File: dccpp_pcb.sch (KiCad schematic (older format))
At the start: 53 parts, among them J1 USB_B_Micro, J10 OSTTC022162, J11 OSTTC022162, J12 OSTTC022162, J2 AVR-ISP-6, J3 OSTTC022162, J4 OSTTC022162, J5 OSTTC022162, J6 OSTTC022162, J7 OSTTC022162, J8 OSTTC022162, J9 OSTTC022162, U1 ATmega32U4-AU, U2 74HC04, U3 IFX007T, U4 IFX007T, U5 IFX007T, U6 IFX007T, Y1 Crystal_Small

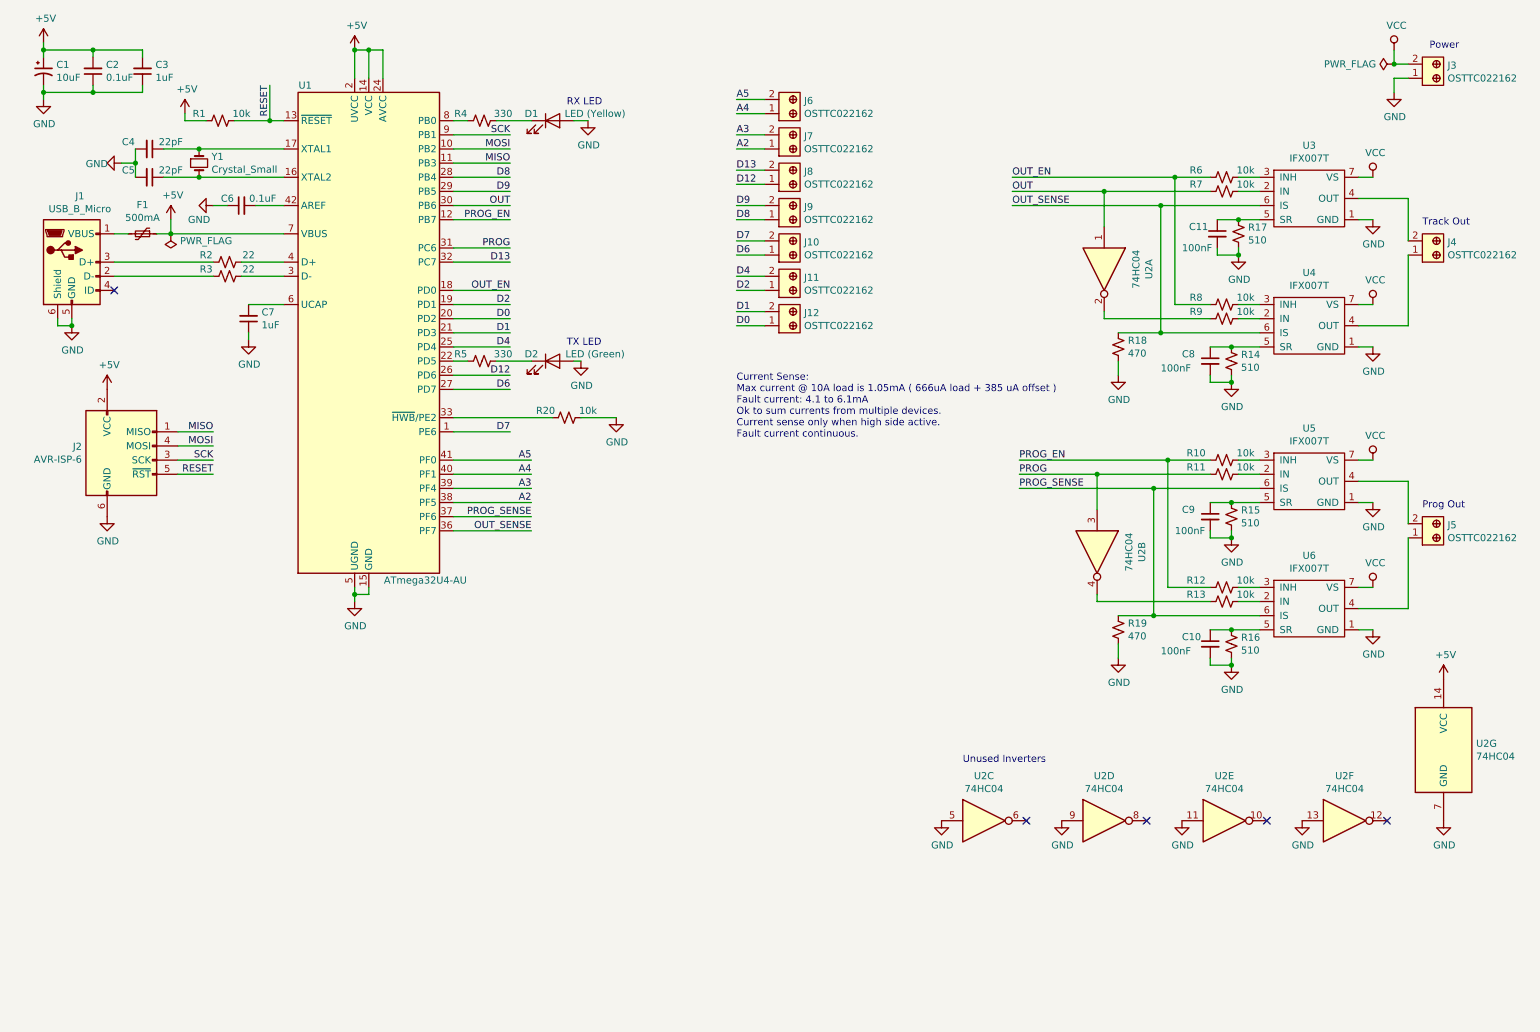
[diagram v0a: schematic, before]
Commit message: Start assigning footprints and part numbers
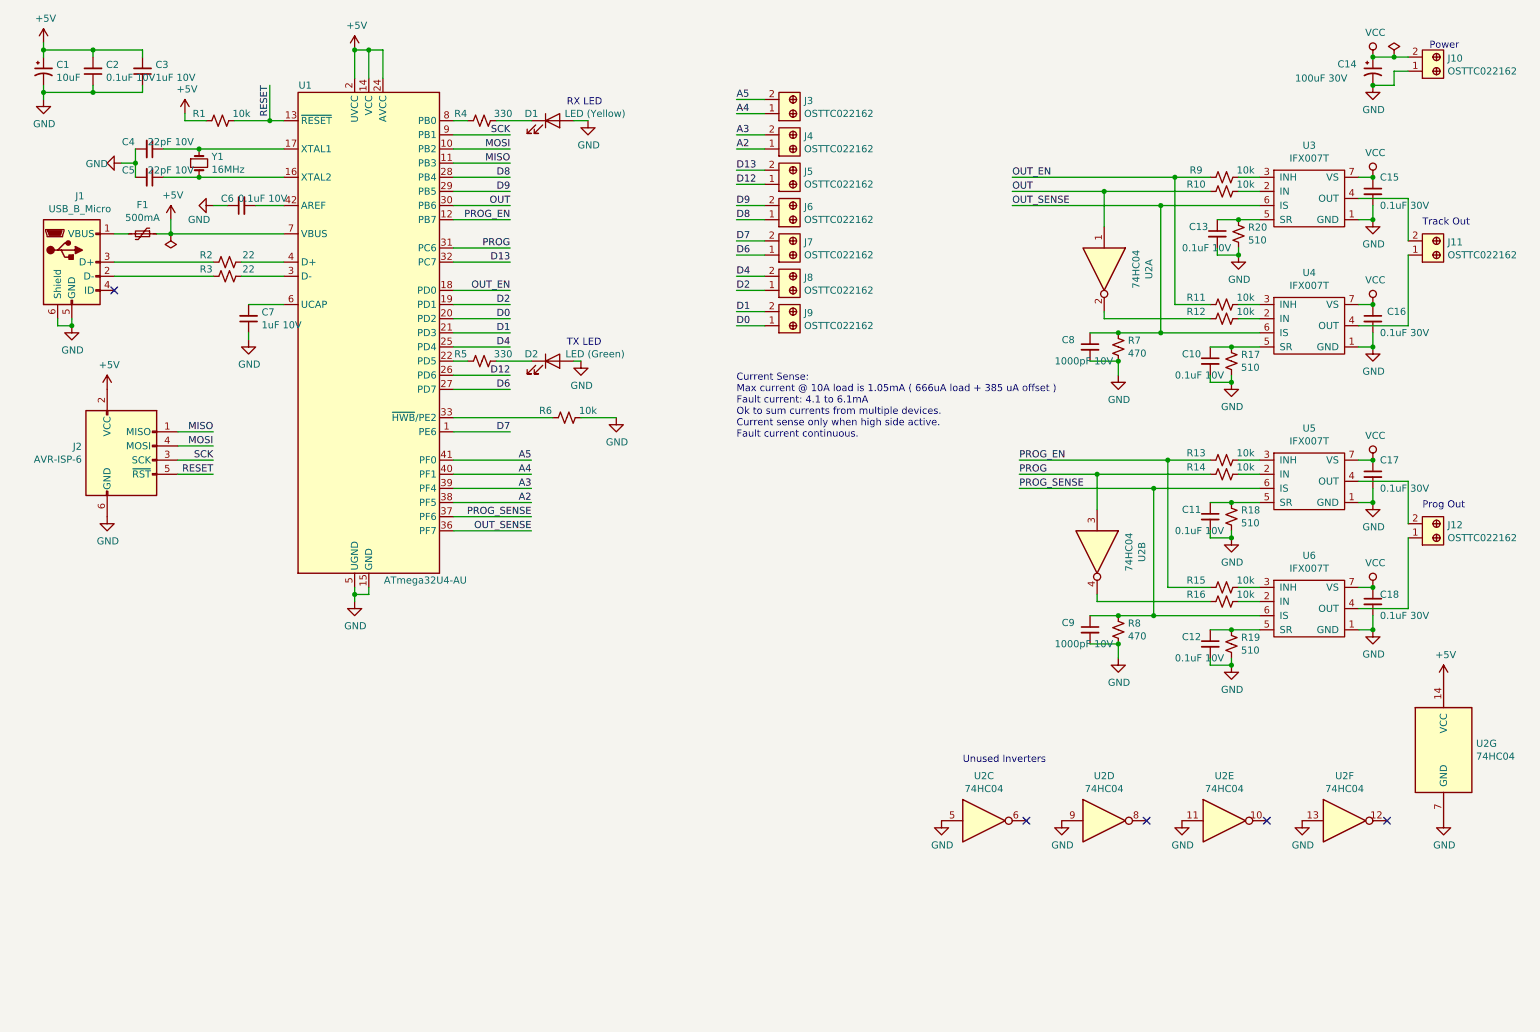
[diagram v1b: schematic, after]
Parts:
- added C14: 100uF 30V, symbol Device:CP1_Small
- added C15, C16, C17, C18: 0.1uF 30V, Capacitor_SMD:C_0603_1608Metric_Pad1.05x0.95mm_HandSolder, symbol Device:C_Small
- added C8, C9: 1000pF 10V, Capacitor_SMD:C_0603_1608Metric_Pad1.05x0.95mm_HandSolder, symbol Device:C_Small
- C1: footprint (none) -> Capacitor_SMD:CP_Elec_4x5.4; Digi-Key_PN (none) -> 732-6401-1-ND; MPN (none) -> 875105240001
- C10: renamed from C8; value 100nF -> 0.1uF 10V; Digi-Key_PN (none) -> 1276-1000-1-ND; MPN (none) -> CL10B104KB8NNNC
- C11: renamed from C9; value 100nF -> 0.1uF 10V; Digi-Key_PN (none) -> 1276-1000-1-ND; MPN (none) -> CL10B104KB8NNNC
- C12: renamed from C10; value 100nF -> 0.1uF 10V; Digi-Key_PN (none) -> 1276-1000-1-ND; MPN (none) -> CL10B104KB8NNNC
- C13: renamed from C11; value 100nF -> 0.1uF 10V; Digi-Key_PN (none) -> 1276-1000-1-ND; MPN (none) -> CL10B104KB8NNNC
- C2, C6: value 0.1uF -> 0.1uF 10V; Digi-Key_PN (none) -> 1276-1000-1-ND; MPN (none) -> CL10B104KB8NNNC
- C3, C7: value 1uF -> 1uF 10V
- C4, C5: value 22pF -> 22pF 10V
- J1: footprint (none) -> Connector_USB:USB_Micro-B_Molex-105017-0001; Digi-Key_PN (none) -> WM1399CT-ND; MPN (none) -> 1050170001
- U1: Digi-Key_PN (none) -> ATMEGA32U4-AU-ND; MPN (none) -> ATMEGA32U4-AU
- U2: footprint (none) -> Package_SO:SOIC-14_3.9x8.7mm_P1.27mm; Digi-Key_PN (none) -> MC74HC04ADGOS-ND; MPN (none) -> MC74HC04ADG
- U3, U4, U5, U6: Digi-Key_PN (none) -> IFX007TAUMA1CT-ND; MPN (none) -> IFX007TAUMA1
- Y1: value Crystal_Small -> 16MHz; footprint (none) -> Crystal:Crystal_SMD_SeikoEpson_TSX3225-4Pin_3.2x2.5mm_HandSoldering; Digi-Key_PN (none) -> SER4069CT-ND; MPN (none) -> TSX-3225 16.0000MF09Z-AC0
- renumbered J3 to J10, J4 to J11, J5 to J12, J6 to J3, J7 to J4, J8 to J5, J9 to J6, J10 to J7, J11 to J8, J12 to J9, R7 to R10, R8 to R11, R9 to R12, R10 to R13, R11 to R14, R12 to R15, R13 to R16, R14 to R17, R15 to R18, R16 to R19, R17 to R20, R20 to R6, R18 to R7, R19 to R8, R6 to R9
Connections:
- net GND: now also C14.2, C15.2, C16.2, C17.2, C18.2, C8.2, C9.2
- net OUT_SENSE: now also C8.1
- net PROG_SENSE: now also C9.1
- net VCC: now also C14.1, C15.1, C16.1, C17.1, C18.1
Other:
- moved on the sheet: J10

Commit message: More part numbers and footprints
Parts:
- C14: footprint (none) -> Capacitor_SMD:CP_Elec_10x10.5; Digi-Key_PN (none) -> 565-4786-1-ND; MPN (none) -> HHXC500ARA101MJA0G
- C3, C7: Digi-Key_PN (none) -> 1276-1182-1-ND; MPN (none) -> CL10A105KP8NNNC
- C4, C5: Digi-Key_PN (none) -> 478-1167-1-ND; MPN (none) -> 06035A220JAT2A
- C8, C9: Digi-Key_PN (none) -> 1276-1018-1-ND; MPN (none) -> CL10B102KB8NNNC
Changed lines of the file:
@@
 F 2 "Capacitor_SMD:C_0603_1608Metric_Pad1.05x0.95mm_HandSolder" H 1450 1700 50  0001 C CNN
 F 3 "~" H 1450 1700 50  0001 C CNN
+F 4 "478-1167-1-ND" H 1450 1700 50  0001 C CNN "Digi-Key_PN"
+F 5 "06035A220JAT2A" H 1450 1700 50  0001 C CNN "MPN"
 	1    1450 1700
 	0    1    1    0
@@
 F 2 "Capacitor_SMD:C_0603_1608Metric_Pad1.05x0.95mm_HandSolder" H 1450 1500 50  0001 C CNN
 F 3 "~" H 1450 1500 50  0001 C CNN
+F 4 "478-1167-1-ND" H 1450 1500 50  0001 C CNN "Digi-Key_PN"
+F 5 "06035A220JAT2A" H 1450 1500 50  0001 C CNN "MPN"
 	1    1450 1500
 	0    1    1    0
@@
 F 2 "Capacitor_SMD:C_0603_1608Metric_Pad1.05x0.95mm_HandSolder" H 2150 2700 50  0001 C CNN
 F 3 "~" H 2150 2700 50  0001 C CNN
+F 4 "1276-1182-1-ND" H 2150 2700 50  0001 C CNN "Digi-Key_PN"
+F 5 "CL10A105KP8NNNC" H 2150 2700 50  0001 C CNN "MPN"
 	1    2150 2700
 	-1   0    0    1
@@
 F 2 "Capacitor_SMD:C_0603_1608Metric_Pad1.05x0.95mm_HandSolder" H 1400 950 50  0001 C CNN
 F 3 "~" H 1400 950 50  0001 C CNN
+F 4 "1276-1182-1-ND" H 1400 950 50  0001 C CNN "Digi-Key_PN"
+F 5 "CL10A105KP8NNNC" H 1400 950 50  0001 C CNN "MPN"
 	1    1400 950
 	-1   0    0    1
@@
 F 2 "Capacitor_SMD:C_0603_1608Metric_Pad1.05x0.95mm_HandSolder" H 8100 4900 50  0001 C CNN
 F 3 "~" H 8100 4900 50  0001 C CNN
+F 4 "1276-1018-1-ND" H 8100 4900 50  0001 C CNN "Digi-Key_PN"
+F 5 "CL10B102KB8NNNC" H 8100 4900 50  0001 C CNN "MPN"
 	1    8100 4900
 	1    0    0    -1
@@
 F 2 "Capacitor_SMD:C_0603_1608Metric_Pad1.05x0.95mm_HandSolder" H 8100 2900 50  0001 C CNN
 F 3 "~" H 8100 2900 50  0001 C CNN
+F 4 "1276-1018-1-ND" H 8100 2900 50  0001 C CNN "Digi-Key_PN"
+F 5 "CL10B102KB8NNNC" H 8100 2900 50  0001 C CNN "MPN"
 	1    8100 2900
 	1    0    0    -1
@@
 F 0 "C14" H 9850 1000 50  0000 L CNN
 F 1 "100uF 30V" H 9550 900 50  0000 L CNN
-F 2 "" H 10100 950 50  0001 C CNN
+F 2 "Capacitor_SMD:CP_Elec_10x10.5" H 10100 950 50  0001 C CNN
 F 3 "~" H 10100 950 50  0001 C CNN
+F 4 "565-4786-1-ND" H 10100 950 50  0001 C CNN "Digi-Key_PN"
+F 5 "HHXC500ARA101MJA0G" H 10100 950 50  0001 C CNN "MPN"
 	1    10100 950
 	1    0    0    -1

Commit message: Final part numbers
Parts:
- D1: Digi-Key_PN (none) -> 732-12018-1-ND; MPN (none) -> 150060YS55040
- D2: Digi-Key_PN (none) -> 732-12017-1-ND; MPN (none) -> 150060VS55040
- F1: value 500mA -> 500mA cont / 1A trip; footprint (none) -> Fuse:Fuse_1206_3216Metric_Pad1.42x1.75mm_HandSolder; Digi-Key_PN (none) -> 507-1802-1-ND; MPN (none) -> 0ZCJ0050FF2G
- J2: Digi-Key_PN (none) -> 609-5122-ND; MPN (none) -> 75869-331LF
- R1, R10, R11, R12, R13, R14, R15, R16, R6, R9: Digi-Key_PN (none) -> RNCP0603FTD10K0CT-ND; MPN (none) -> RNCP0603FTD10K0
- R17, R18, R19, R20: Digi-Key_PN (none) -> 311-510HRCT-ND; MPN (none) -> RC0603FR-07510RL
- R2, R3: Digi-Key_PN (none) -> 311-22.0HRCT-ND; MPN (none) -> RC0603FR-0722RL
- R4, R5: Digi-Key_PN (none) -> 311-330HRCT-ND; MPN (none) -> RC0603FR-07330RL
- R7, R8: Digi-Key_PN (none) -> 311-470HRCT-ND; MPN (none) -> RC0603FR-07470RL
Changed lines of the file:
@@
 F 2 "Resistor_SMD:R_0603_1608Metric_Pad1.05x0.95mm_HandSolder" H 2000 2400 50  0001 C CNN
 F 3 "~" H 2000 2400 50  0001 C CNN
+F 4 "311-22.0HRCT-ND" H 2000 2400 50  0001 C CNN "Digi-Key_PN"
+F 5 "RC0603FR-0722RL" H 2000 2400 50  0001 C CNN "MPN"
 	1    2000 2400
 	0    1    1    0
@@
 P 1400 2100
 F 0 "F1" V 1195 2100 50  0000 C CNN
-F 1 "500mA" V 1286 2100 50  0000 C CNN
-F 2 "" H 1450 1900 50  0001 L CNN
+F 1 "500mA cont / 1A trip" V 1286 2100 50  0000 C CNN
+F 2 "Fuse:Fuse_1206_3216Metric_Pad1.42x1.75mm_HandSolder" H 1450 1900 50  0001 L CNN
 F 3 "~" H 1400 2100 50  0001 C CNN
+F 4 "507-1802-1-ND" H 1400 2100 50  0001 C CNN "Digi-Key_PN"
+F 5 "0ZCJ0050FF2G" H 1400 2100 50  0001 C CNN "MPN"
 	1    1400 2100
 	0    1    1    0
@@
 F 2 "Resistor_SMD:R_0603_1608Metric_Pad1.05x0.95mm_HandSolder" H 1950 1300 50  0001 C CNN
 F 3 "~" H 1950 1300 50  0001 C CNN
+F 4 "RNCP0603FTD10K0CT-ND" H 1950 1300 50  0001 C CNN "Digi-Key_PN"
+F 5 "RNCP0603FTD10K0" H 1950 1300 50  0001 C CNN "MPN"
 	1    1950 1300
 	0    1    1    0
@@
 F 2 "Resistor_SMD:R_0603_1608Metric_Pad1.05x0.95mm_HandSolder" H 2000 2300 50  0001 C CNN
 F 3 "~" H 2000 2300 50  0001 C CNN
+F 4 "311-22.0HRCT-ND" H 2000 2300 50  0001 C CNN "Digi-Key_PN"
+F 5 "RC0603FR-0722RL" H 2000 2300 50  0001 C CNN "MPN"
 	1    2000 2300
 	0    1    1    0
@@
 F 2 "Connector_IDC:IDC-Header_2x03_P2.54mm_Vertical" V 1000 3750 50  0001 C CNN
 F 3 " ~" H -25 3150 50  0001 C CNN
+F 4 "609-5122-ND" H 1250 3700 50  0001 C CNN "Digi-Key_PN"
+F 5 "75869-331LF" H 1250 3700 50  0001 C CNN "MPN"
 	1    1250 3700
 	1    0    0    -1
@@
 F 2 "Resistor_SMD:R_0603_1608Metric_Pad1.05x0.95mm_HandSolder" H 9150 2100 50  0001 C CNN
 F 3 "~" H 9150 2100 50  0001 C CNN
+F 4 "311-510HRCT-ND" H 9150 2100 50  0001 C CNN "Digi-Key_PN"
+F 5 "RC0603FR-07510RL" H 9150 2100 50  0001 C CNN "MPN"
 	1    9150 2100
 	1    0    0    -1
@@
 F 2 "Resistor_SMD:R_0603_1608Metric_Pad1.05x0.95mm_HandSolder" H 9100 3000 50  0001 C CNN
 F 3 "~" H 9100 3000 50  0001 C CNN
+F 4 "311-510HRCT-ND" H 9100 3000 50  0001 C CNN "Digi-Key_PN"
+F 5 "RC0603FR-07510RL" H 9100 3000 50  0001 C CNN "MPN"
 	1    9100 3000
 	1    0    0    -1
@@
 F 2 "Resistor_SMD:R_0603_1608Metric_Pad1.05x0.95mm_HandSolder" H 9100 4100 50  0001 C CNN
 F 3 "~" H 9100 4100 50  0001 C CNN
+F 4 "311-510HRCT-ND" H 9100 4100 50  0001 C CNN "Digi-Key_PN"
+F 5 "RC0603FR-07510RL" H 9100 4100 50  0001 C CNN "MPN"
 	1    9100 4100
 	1    0    0    -1
@@
 F 2 "Resistor_SMD:R_0603_1608Metric_Pad1.05x0.95mm_HandSolder" H 9100 5000 50  0001 C CNN
 F 3 "~" H 9100 5000 50  0001 C CNN
+F 4 "311-510HRCT-ND" H 9100 5000 50  0001 C CNN "Digi-Key_PN"
+F 5 "RC0603FR-07510RL" H 9100 5000 50  0001 C CNN "MPN"
 	1    9100 5000
 	1    0    0    -1
@@
 F 2 "Resistor_SMD:R_0603_1608Metric_Pad1.05x0.95mm_HandSolder" H 9050 1700 50  0001 C CNN
 F 3 "~" H 9050 1700 50  0001 C CNN
+F 4 "RNCP0603FTD10K0CT-ND" H 9050 1700 50  0001 C CNN "Digi-Key_PN"
+F 5 "RNCP0603FTD10K0" H 9050 1700 50  0001 C CNN "MPN"
 	1    9050 1700
 	0    1    1    0
@@
 F 2 "Resistor_SMD:R_0603_1608Metric_Pad1.05x0.95mm_HandSolder" H 9050 1800 50  0001 C CNN
 F 3 "~" H 9050 1800 50  0001 C CNN
+F 4 "RNCP0603FTD10K0CT-ND" H 9050 1800 50  0001 C CNN "Digi-Key_PN"
+F 5 "RNCP0603FTD10K0" H 9050 1800 50  0001 C CNN "MPN"
 	1    9050 1800
 	0    1    1    0
@@
 F 2 "Resistor_SMD:R_0603_1608Metric_Pad1.05x0.95mm_HandSolder" H 9050 2600 50  0001 C CNN
 F 3 "~" H 9050 2600 50  0001 C CNN
+F 4 "RNCP0603FTD10K0CT-ND" H 9050 2600 50  0001 C CNN "Digi-Key_PN"
+F 5 "RNCP0603FTD10K0" H 9050 2600 50  0001 C CNN "MPN"
 	1    9050 2600
 	0    1    1    0
@@
 F 2 "Resistor_SMD:R_0603_1608Metric_Pad1.05x0.95mm_HandSolder" H 9050 2700 50  0001 C CNN
 F 3 "~" H 9050 2700 50  0001 C CNN
+F 4 "RNCP0603FTD10K0CT-ND" H 9050 2700 50  0001 C CNN "Digi-Key_PN"
+F 5 "RNCP0603FTD10K0" H 9050 2700 50  0001 C CNN "MPN"
 	1    9050 2700
 	0    1    1    0
@@
 F 2 "Resistor_SMD:R_0603_1608Metric_Pad1.05x0.95mm_HandSolder" H 9050 3700 50  0001 C CNN
 F 3 "~" H 9050 3700 50  0001 C CNN
+F 4 "RNCP0603FTD10K0CT-ND" H 9050 3700 50  0001 C CNN "Digi-Key_PN"
+F 5 "RNCP0603FTD10K0" H 9050 3700 50  0001 C CNN "MPN"
 	1    9050 3700
 	0    1    1    0
@@
 F 2 "Resistor_SMD:R_0603_1608Metric_Pad1.05x0.95mm_HandSolder" H 9050 3800 50  0001 C CNN
 F 3 "~" H 9050 3800 50  0001 C CNN
+F 4 "RNCP0603FTD10K0CT-ND" H 9050 3800 50  0001 C CNN "Digi-Key_PN"
+F 5 "RNCP0603FTD10K0" H 9050 3800 50  0001 C CNN "MPN"
 	1    9050 3800
 	0    1    1    0
@@
 F 2 "Resistor_SMD:R_0603_1608Metric_Pad1.05x0.95mm_HandSolder" H 9050 4600 50  0001 C CNN
 F 3 "~" H 9050 4600 50  0001 C CNN
+F 4 "RNCP0603FTD10K0CT-ND" H 9050 4600 50  0001 C CNN "Digi-Key_PN"
+F 5 "RNCP0603FTD10K0" H 9050 4600 50  0001 C CNN "MPN"
 	1    9050 4600
 	0    1    1    0
@@
 F 2 "Resistor_SMD:R_0603_1608Metric_Pad1.05x0.95mm_HandSolder" H 9050 4700 50  0001 C CNN
 F 3 "~" H 9050 4700 50  0001 C CNN
+F 4 "RNCP0603FTD10K0CT-ND" H 9050 4700 50  0001 C CNN "Digi-Key_PN"
+F 5 "RNCP0603FTD10K0" H 9050 4700 50  0001 C CNN "MPN"
 	1    9050 4700
 	0    1    1    0
@@
 F 2 "LED_SMD:LED_0603_1608Metric_Pad1.05x0.95mm_HandSolder" H 4300 3000 50  0001 C CNN
 F 3 "~" H 4300 3000 50  0001 C CNN
+F 4 "732-12017-1-ND" H 4300 3000 50  0001 C CNN "Digi-Key_PN"
+F 5 "150060VS55040" H 4300 3000 50  0001 C CNN "MPN"
 	1    4300 3000
 	1    0    0    -1
@@
 F 2 "Resistor_SMD:R_0603_1608Metric_Pad1.05x0.95mm_HandSolder" H 3800 3000 50  0001 C CNN
 F 3 "~" H 3800 3000 50  0001 C CNN
+F 4 "311-330HRCT-ND" H 3800 3000 50  0001 C CNN "Digi-Key_PN"
+F 5 "RC0603FR-07330RL" H 3800 3000 50  0001 C CNN "MPN"
 	1    3800 3000
 	0    1    1    0
@@
 F 2 "Resistor_SMD:R_0603_1608Metric_Pad1.05x0.95mm_HandSolder" H 3800 1300 50  0001 C CNN
 F 3 "~" H 3800 1300 50  0001 C CNN
+F 4 "311-330HRCT-ND" H 3800 1300 50  0001 C CNN "Digi-Key_PN"
+F 5 "RC0603FR-07330RL" H 3800 1300 50  0001 C CNN "MPN"
 	1    3800 1300
 	0    1    1    0
@@
 F 2 "LED_SMD:LED_0603_1608Metric_Pad1.05x0.95mm_HandSolder" H 4300 1300 50  0001 C CNN
 F 3 "~" H 4300 1300 50  0001 C CNN
+F 4 "732-12018-1-ND" H 4300 1300 50  0001 C CNN "Digi-Key_PN"
+F 5 "150060YS55040" H 4300 1300 50  0001 C CNN "MPN"
 	1    4300 1300
 	1    0    0    -1
@@
 F 2 "Resistor_SMD:R_0603_1608Metric_Pad1.05x0.95mm_HandSolder" H 8300 4900 50  0001 C CNN
 F 3 "~" H 8300 4900 50  0001 C CNN
+F 4 "311-470HRCT-ND" H 8300 4900 50  0001 C CNN "Digi-Key_PN"
+F 5 "RC0603FR-07470RL" H 8300 4900 50  0001 C CNN "MPN"
 	1    8300 4900
 	1    0    0    -1
@@
 F 2 "Resistor_SMD:R_0603_1608Metric_Pad1.05x0.95mm_HandSolder" H 8300 2900 50  0001 C CNN
 F 3 "~" H 8300 2900 50  0001 C CNN
+F 4 "311-470HRCT-ND" H 8300 2900 50  0001 C CNN "Digi-Key_PN"
+F 5 "RC0603FR-07470RL" H 8300 2900 50  0001 C CNN "MPN"
 	1    8300 2900
 	1    0    0    -1
@@
 F 2 "Resistor_SMD:R_0603_1608Metric_Pad1.05x0.95mm_HandSolder" H 4400 3400 50  0001 C CNN
 F 3 "~" H 4400 3400 50  0001 C CNN
+F 4 "RNCP0603FTD10K0CT-ND" H 4400 3400 50  0001 C CNN "Digi-Key_PN"
+F 5 "RNCP0603FTD10K0" H 4400 3400 50  0001 C CNN "MPN"
 	1    4400 3400
 	0    1    1    0
